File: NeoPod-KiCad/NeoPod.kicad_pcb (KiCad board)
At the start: 2 copper layers, 9.2 x 6.6 mm, 21 parts, among them J4 USB4500-03-0-A_REVA1, SW1 SW_SPST, SW2 SW_SPST, SW3 SW_SPST, SW4 SW_SPST, SW5 SW_SPST, U1 ESP32-WROOM-32, U2 PCM5102A, U3 RP2040, U4 CP2102N-Axx-xQFN24, U8 STC4054GR, Y2 40MHz-Xtal

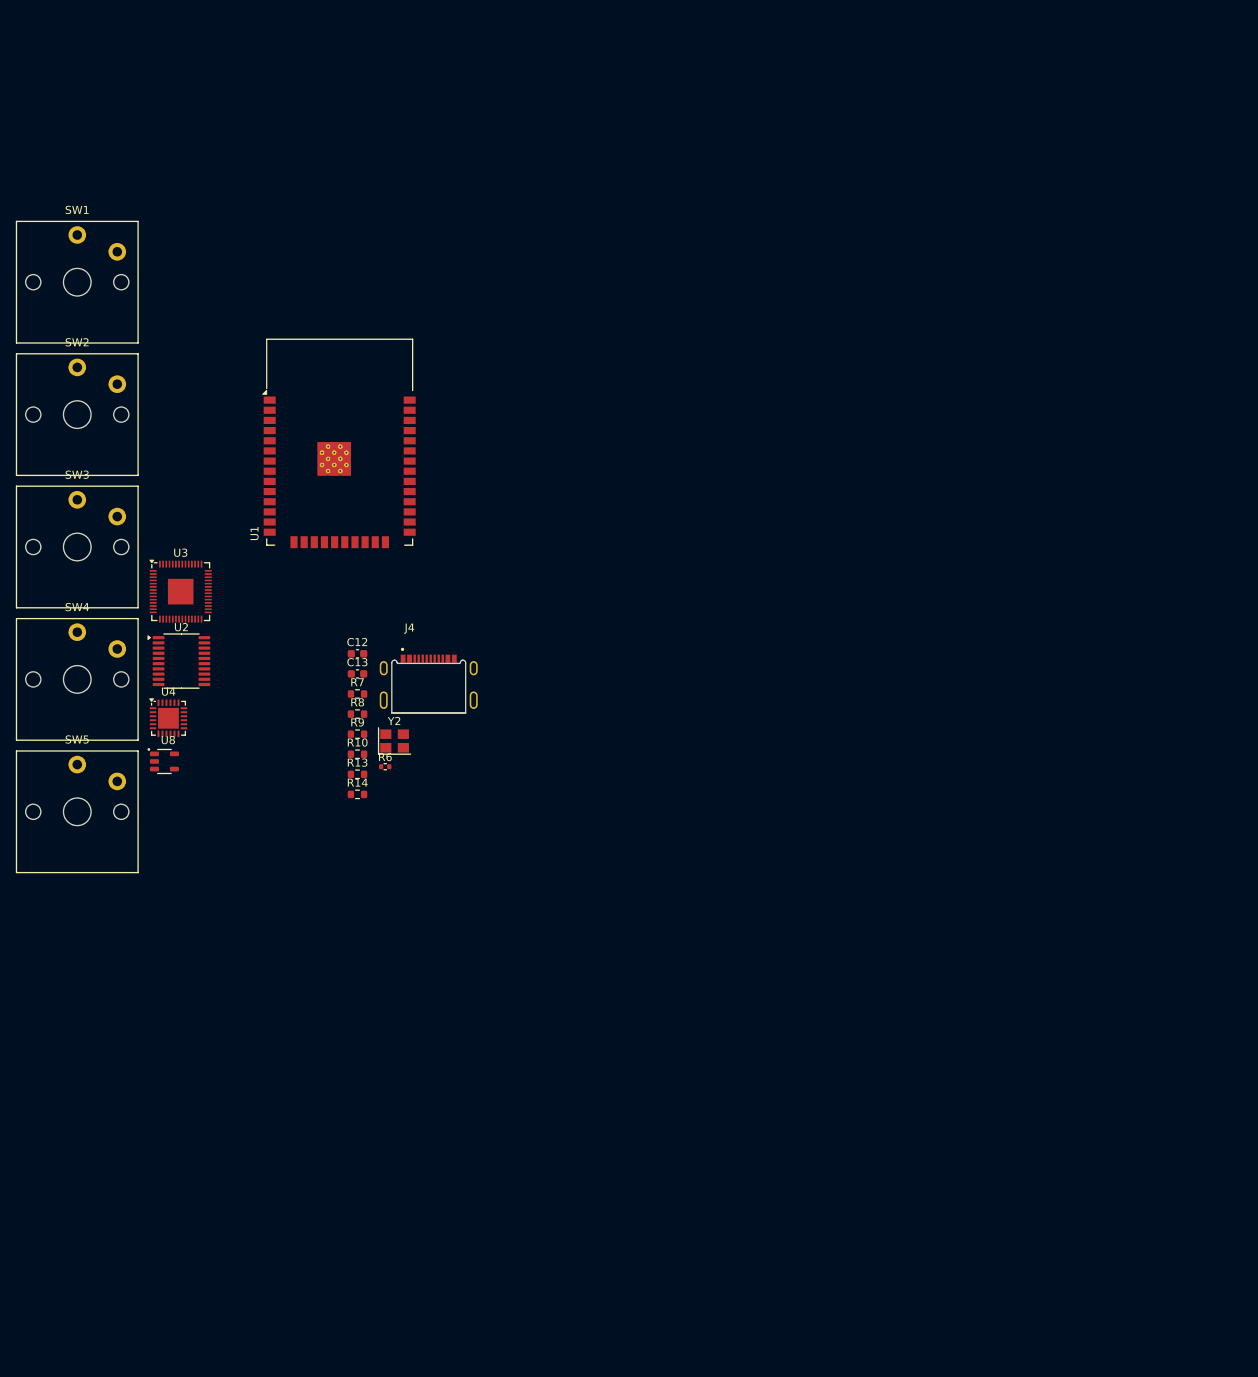
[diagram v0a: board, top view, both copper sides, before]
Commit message: Started pcb layout and added images
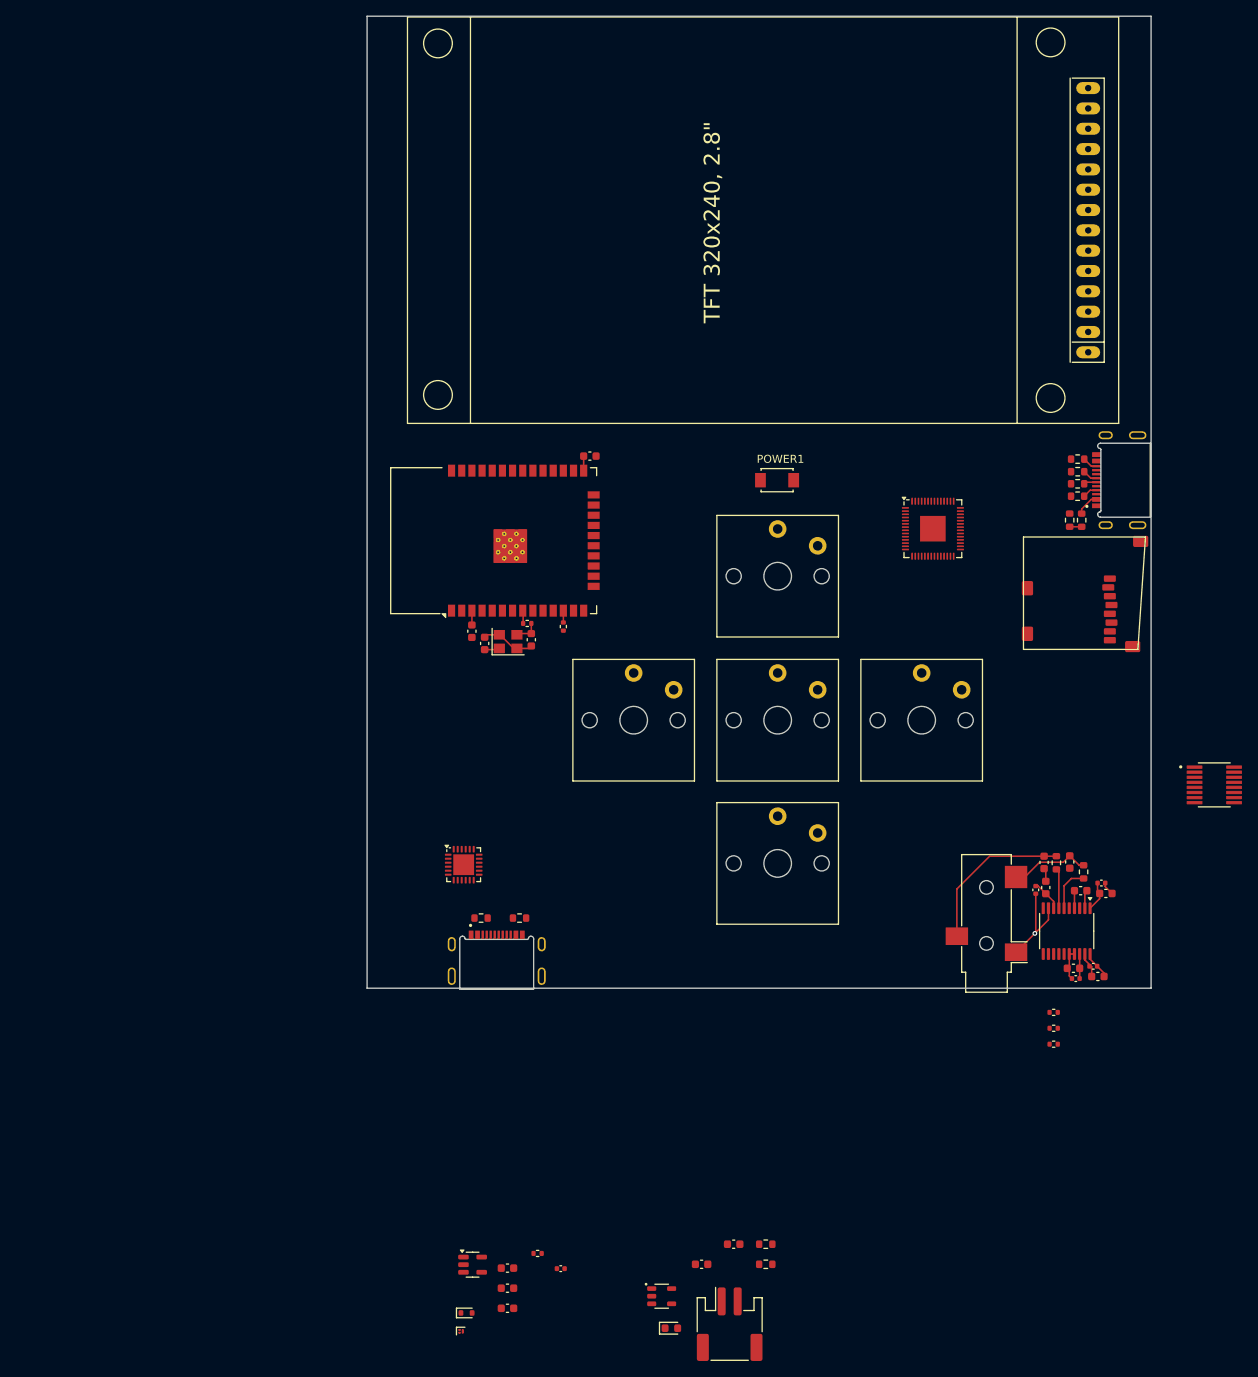
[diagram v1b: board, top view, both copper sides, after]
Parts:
- removed U8: STC4054GR, STC4054GR:SOT95P280X110-5N
- added BT1: Battery_Cell, Connector_JST:JST_PH_S2B-PH-SM4-TB_1x02-1MP_P2.00mm_Horizontal, F.Cu at (149.5, 187.5)
- added C1: 0.1uF, Capacitor_SMD:C_0603_1608Metric, F.Cu at (189.0, 132.9)
- added C10: 0.1uF, Capacitor_SMD:C_0603_1608Metric, F.Cu at (196.5, 133.7)
- added C11: 10uF, Capacitor_SMD:C_0402_1005Metric, F.Cu at (196.0, 132.4)
- added C14: 0.1uF, Capacitor_SMD:C_0603_1608Metric, F.Cu at (132.0, 79.0)
- added C15: 0.1uF, Capacitor_SMD:C_0603_1608Metric, F.Cu at (117.3, 100.9)
- added C2: 10uF, Capacitor_SMD:C_0402_1005Metric, F.Cu at (187.8, 133.2)
- added C24: 2.2uF, Capacitor_SMD:C_0603_1608Metric, F.Cu at (146.0, 180.0)
- added C26: 100nF, Capacitor_SMD:C_0402_1005Metric, F.Cu at (128.4, 180.6)
- added C27: 2.2uF, Capacitor_SMD:C_0603_1608Metric, F.Cu at (121.7, 180.5)
- added C28: 2.2uF, Capacitor_SMD:C_0603_1608Metric, F.Cu at (121.7, 183.0)
- added C29: 2.2uF, Capacitor_SMD:C_0603_1608Metric, F.Cu at (121.7, 185.5)
- added C3: 2.2nF, Capacitor_SMD:C_0603_1608Metric, F.Cu at (192.0, 129.7)
- added C30: 2.2uF, Capacitor_SMD:C_0603_1608Metric, F.Cu at (150.0, 177.5)
- added C4: 2.2nF, Capacitor_SMD:C_0603_1608Metric, F.Cu at (188.8, 129.8)
- added C5: 2.2uF, Capacitor_SMD:C_0603_1608Metric, F.Cu at (193.4, 133.3)
- added C6: 10uF, Capacitor_SMD:C_0402_1005Metric, F.Cu at (192.8, 144.3)
- added C7: 0.1uF, Capacitor_SMD:C_0603_1608Metric, F.Cu at (192.5, 143.0)
- added C8: 10uF, Capacitor_SMD:C_0402_1005Metric, F.Cu at (195.0, 142.8)
- added C9: 0.1uF, Capacitor_SMD:C_0603_1608Metric, F.Cu at (195.5, 144.0)
- added D1: MSK4005, Diode_SMD:D_SOD-523, F.Cu at (116.6, 186.1)
- added D2: LED, LED_SMD:LED_0603_1608Metric, F.Cu at (142.2, 188.0)
- added J1: SJ-3523-SMT-TR, Connector_Audio:Jack_3.5mm_CUI_SJ-3523-SMT_Horizontal, F.Cu at (181.6, 137.4)
- added J2: USB4500-03-0-A_REVA1, USB-C-2.0-24P(16+8):GCT_USB4500-03-0-A_REVA1, F.Cu at (120.4, 144.0)
- added POWER1: SW6, SW_TS-1088-AR2016:SW_TS-1088-AR02016, F.Cu at (155.4, 82.0)
- added Q1: CSD25480F3, Package_DFN_QFN:Texas_PicoStar_DFN-3_0.69x0.60mm, F.Cu at (115.9, 188.4)
- added R1: 470, Resistor_SMD:R_0603_1608Metric, F.Cu at (190.3, 129.8)
- added R11: 10k, Resistor_SMD:R_0603_1608Metric, F.Cu at (193.5, 87.0)
- added R12: 20k, Resistor_SMD:R_0603_1608Metric, F.Cu at (192.0, 87.0)
- added R15: 100k, Resistor_SMD:R_0402_1005Metric, F.Cu at (125.5, 178.7)
- added R16: 2.7k, Resistor_SMD:R_0603_1608Metric, F.Cu at (154.0, 177.5)
- added R17: 2.2k, Resistor_SMD:R_0603_1608Metric, F.Cu at (154.0, 180.0)
- added R18: 100, Resistor_SMD:R_0402_1005Metric, F.Cu at (128.7, 100.3)
- added R2: 470, Resistor_SMD:R_0603_1608Metric, F.Cu at (193.7, 131.0)
- added R3: 22, Resistor_SMD:R_0402_1005Metric, F.Cu at (190.0, 148.5)
- added R4: 22, Resistor_SMD:R_0402_1005Metric, F.Cu at (190.0, 150.5)
- added R5: 22, Resistor_SMD:R_0402_1005Metric, F.Cu at (190.0, 152.5)
- added U10: SN74CB3Q3257DBQR, SN74CB3Q3257DBQR:SN74CB3Q3257DBQR, F.Cu at (210.1, 120.1)
- added U5: XC6210B332MR, Package_TO_SOT_SMD:SOT-23-5, F.Cu at (117.4, 180.1)
- added U6: STC4054GR, STC4054GR:SOT95P280X110-5N, F.Cu at (141.0, 184.0)
- added U7: TFT_320x240, TFT-320x240:TFT-320x240, F.Cu at (194.3, 49.5)
- added X1: ~, Adafruit_MicroSD_Socket:MicroSD_Socket, F.Cu at (194.0, 96.1)
- moved U2 115.7 mm to (191.6, 138.4), turned to -90 degrees
- moved SW3 107.7 mm to (173.5, 112.0)
- moved R9 96.4 mm to (193.0, 79.4)
- moved R10 95.6 mm to (193.0, 84.0), turned to 180 degrees
- moved SW2 95.5 mm to (155.5, 112.0)
- moved R8 95.0 mm to (193.0, 80.9), turned to 180 degrees
- moved U3 94.3 mm to (174.9, 88.1)
- moved R7 93.8 mm to (193.0, 82.4), turned to 180 degrees
- moved J4 92.8 mm to (200.5, 82.0), turned to 90 degrees
- moved SW1 88.5 mm to (137.5, 112.0)
- moved SW4 88.5 mm to (155.5, 94.0)
- moved SW5 87.8 mm to (155.5, 129.9)
- moved U4 41.2 mm to (116.2, 130.1)
- moved R14 25.5 mm to (123.2, 136.7)
- moved R6 25.2 mm to (124.2, 99.9), turned to 180 degrees
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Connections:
- SW1 pad 1: unconnected-(SW1-A-Pad1) -> SW1
- SW1 pad 2: unconnected-(SW1-B-Pad2) -> GND
- SW2 pad 1: unconnected-(SW2-A-Pad1) -> SW2
- SW2 pad 2: unconnected-(SW2-B-Pad2) -> GND
- SW3 pad 1: unconnected-(SW3-A-Pad1) -> SW3
- SW3 pad 2: unconnected-(SW3-B-Pad2) -> GND
- SW4 pad 1: unconnected-(SW4-A-Pad1) -> SW4
- SW4 pad 2: unconnected-(SW4-B-Pad2) -> GND
- SW5 pad 1: unconnected-(SW5-A-Pad1) -> SW5
- SW5 pad 2: unconnected-(SW5-B-Pad2) -> GND
- U1 pad 1: AGND -> GND
- U1 pad 12: unconnected-(U1-IO27-Pad12) -> Net-(U1-IO27)
- U1 pad 13: unconnected-(U1-IO14-Pad13) -> SCK-TFT
- U1 pad 14: unconnected-(U1-IO12-Pad14) -> MISO-TFT
- U1 pad 15: AGND -> GND
- U1 pad 16: unconnected-(U1-IO13-Pad16) -> MOSI-TFT
- U1 pad 23: unconnected-(U1-IO15-Pad23) -> SW3
- U1 pad 24: unconnected-(U1-IO2-Pad24) -> SW1
- U1 pad 26: unconnected-(U1-IO4-Pad26) -> SW2
- U1 pad 27: unconnected-(U1-IO16-Pad27) -> SW4
- U1 pad 28: unconnected-(U1-IO17-Pad28) -> SW5
- U1 pad 29: unconnected-(U1-IO5-Pad29) -> CS-TFT
- U1 pad 38: AGND -> GND
- U1 pad 39: AGND -> GND
- U1 pad 6: unconnected-(U1-IO34-Pad6) -> DC-TFT
- U1 pad 7: unconnected-(U1-IO35-Pad7) -> Net-(POWER1-A)
- U2 pad 10: AGND -> GND
- U2 pad 11: AGND -> GND
- U2 pad 16: AGND -> GND
- U2 pad 17: AGND -> GND
- U3 pad 1: Net-(U3-IOVDD-Pad1) -> unconnected-(U3-IOVDD-Pad1)_3
- U3 pad 10: Net-(U3-IOVDD-Pad1) -> unconnected-(U3-IOVDD-Pad1)_2
- U3 pad 22: Net-(U3-IOVDD-Pad1) -> unconnected-(U3-IOVDD-Pad1)_1
- U3 pad 23: Net-(U3-DVDD-Pad23) -> unconnected-(U3-DVDD-Pad23)_1
- U3 pad 33: Net-(U3-IOVDD-Pad1) -> unconnected-(U3-IOVDD-Pad1)
- U3 pad 42: Net-(U3-IOVDD-Pad1) -> unconnected-(U3-IOVDD-Pad1)_5
- U3 pad 49: Net-(U3-IOVDD-Pad1) -> unconnected-(U3-IOVDD-Pad1)_4
- U3 pad 50: Net-(U3-DVDD-Pad23) -> unconnected-(U3-DVDD-Pad23)
- U3 pad 57: AGND -> GND
- U4 pad 2: AGND -> GND
- U4 pad 25: AGND -> GND
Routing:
- net Net-(C4-Pad1): track 0.00 -> 20.0 mm
- net GNDREF: track 0.00 -> 15.4 mm, vias 0 -> 1
- net GND: track 0.00 -> 10.6 mm
- net Net-(C3-Pad2): track 0.00 -> 10.0 mm
- net VCC3v3a: track 0.00 -> 7.63 mm
- net Net-(U2-OUTL): track 0.00 -> 5.62 mm
- net Net-(U2-OUTR): track 0.00 -> 4.98 mm
- net VCC3v3: track 0.00 -> 3.53 mm
- net AGND: track 0.00 -> 3.16 mm
- net Net-(C12-Pad2): track 0.00 -> 3.13 mm
- net Net-(U2-LDOO): track 0.00 -> 3.08 mm
- net VBUS-RP2040: track 0.00 -> 2.88 mm
- net Net-(U2-CAPP): track 0.00 -> 2.29 mm
- net Net-(U2-CAPM): track 0.00 -> 2.19 mm
- net Net-(U1-IO33): track 0.00 -> 1.89 mm
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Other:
- board size 9.2 x 6.6 mm -> 98 x 121.5 mm
- copper layers 2 -> 4

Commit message: finished pcb
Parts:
- moved X1 88.5 mm to (112.2, 129.9), turned to 90 degrees
- moved Q1 82.5 mm to (170.5, 126.6), turned to 90 degrees
- moved U7 82.0 mm to (112.4, 49.5), turned to -90 degrees
- moved U6 80.0 mm to (185.4, 117.5)
- moved D2 78.9 mm to (185.0, 121.7)
- moved BT1 78.6 mm to (191.3, 121.0), turned to 90 degrees
- moved D1 77.6 mm to (169.4, 129.2), turned to 180 degrees
- moved C28 73.7 mm to (172.4, 129.5)
- moved C27 73.0 mm to (172.4, 128.0)
- moved C24 71.5 mm to (185.0, 120.1)
- moved U5 71.2 mm to (170.4, 132.6), turned to -90 degrees
- moved C30 71.0 mm to (189.2, 118.2)
- moved R16 70.3 mm to (189.2, 116.7), turned to 180 degrees
- moved C29 69.9 mm to (170.6, 135.6), turned to 180 degrees
- moved R15 67.5 mm to (169.4, 127.4), turned to 90 degrees
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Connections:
- C29 pad 1: VCC_3v3 -> VCC3v3
- C8 pad 2: AGND -> GND
- C9 pad 2: AGND -> GND
- R17 pad 2: VCC_3v3 -> VCC3v3
- U2 pad 19: AGND -> GND
- U5 pad 5: VCC_3v3 -> VCC3v3
- U7 pad 1: VCC_3v3 -> VCC3v3
- U7 pad 4: VCC_3v3 -> VCC3v3
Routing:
- net DIN: track 0.00 -> 113.7 mm, vias 0 -> 2
- net LRCK: track 0.00 -> 90.6 mm
- net GND: track 10.6 -> 98.0 mm, vias 0 -> 14
- net DC-TFT: track 0.00 -> 87.2 mm, vias 0 -> 1
- net BCK: track 0.00 -> 85.6 mm
- net MOSI-SD: track 0.00 -> 81.3 mm, vias 0 -> 2
- net MISO-SD: track 0.00 -> 80.6 mm, vias 0 -> 2
- net MOSI-ESP32: track 0.00 -> 73.1 mm, vias 0 -> 2
- net CS-SD: track 0.00 -> 72.4 mm, vias 0 -> 2
- net SCK-SD: track 0.00 -> 71.2 mm, vias 0 -> 2
- net SCK-TFT: track 0.00 -> 66.7 mm, vias 0 -> 1
- net SW4: track 0.00 -> 63.5 mm
- net RXD-U0TXD: track 0.00 -> 62.1 mm, vias 0 -> 2
- net TXD-U0RXD: track 0.00 -> 61.6 mm, vias 0 -> 2
- net LED-TFT: track 0.00 -> 61.1 mm, vias 0 -> 1
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- added copper zone on In1.Cu, net GND
- added copper zone on In1.Cu, net GNDREF
- added copper zone on In2.Cu, net VCC3v3
- added copper zone on In2.Cu, net VCC3v3a
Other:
- board size 98 x 121.5 mm -> 100 x 120 mm

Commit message: finished pcb
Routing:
- net DIN: track 113.7 -> 115.5 mm
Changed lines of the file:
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@@
+	)
+	(segment
+		(start 129.895 96.555)
+		(end 124.555 96.555)
+		(width 0.2)
+		(layer "F.Cu")
+		(net 89)
 	)
 	(segment
@@
 	)
 	(segment
+		(start 121.05 93.05)
+		(end 121 93.05)
+		(width 0.2)
+		(layer "F.Cu")
+		(net 89)
+	)
+	(segment
 		(start 129.55 137.212858)
 		(end 129.55 135.461171)
@@
 	)
 	(segment
-		(start 124.505 96.555)
-		(end 121 93.05)
-		(width 0.2)
-		(layer "F.Cu")
-		(net 89)
-	)
-	(segment
 		(start 116.268915 102.913304)
 		(end 114.693467 102.913304)
@@
 	)
 	(segment
-		(start 129.895 96.555)
-		(end 124.505 96.555)
-		(width 0.2)
-		(layer "F.Cu")
-		(net 89)
-	)
-	(segment
 		(start 189.936718 118.563282)
 		(end 188.5 120)
@@
 	)
 	(segment
+		(start 124.555 96.555)
+		(end 121.05 93.05)
+		(width 0.2)
+		(layer "F.Cu")
+		(net 89)
+	)
+	(segment
 		(start 189.986718 118.180712)
 		(end 189.936718 118.230712)
@@
 	)
 	(segment
-		(start 114.5 98)
+		(start 114.5 101)
 		(end 114.5 80)
 		(width 0.2)
@@
 	)
 	(segment
-		(start 125 108.5)
-		(end 114.5 98)
+		(start 155.9 142.4)
+		(end 114.5 101)
 		(width 0.2)
 		(layer "In1.Cu")
@@
 	)
 	(segment
-		(start 158.9 142.4)
-		(end 125 108.5)
+		(start 188 142.4)
+		(end 155.9 142.4)
 		(width 0.2)
 		(layer "In1.Cu")
-		(net 114)
-	)
-	(segment
-		(start 188 142.4)
-		(end 158.9 142.4)
-		(width 0.2)
-		(layer "In1.Cu")
